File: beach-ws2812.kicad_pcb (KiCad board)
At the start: 4 copper layers, 260 x 120 mm, 343 parts, among them CON101 BARREL_JACK, P101 CONN_01X03, SW101 Pushbutton, SW102 Pushbutton, U101 STM32F103C(8-B)Tx, U102 LM1117-3.3, U103 MAX811, X101 8MHz

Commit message: Added mounting holes.
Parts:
- added C601: 100nF, Capacitors_SMD:C_0603, F.Cu at (238.4, 99.0)
- added C602: 100nF, Capacitors_SMD:C_0603, F.Cu at (255.6, 101.0)
- added C603: 100nF, Capacitors_SMD:C_0603, F.Cu at (261.2, 110.2)
- added C604: 100nF, Capacitors_SMD:C_0603, F.Cu at (268.8, 120.2)
- added C605: 100nF, Capacitors_SMD:C_0603, F.Cu at (277.8, 103.6)
- added C606: 100nF, Capacitors_SMD:C_0603, F.Cu at (277.4, 92.2)
- added C607: 100nF, Capacitors_SMD:C_0603, F.Cu at (262.0, 87.4)
- added C608: 100nF, Capacitors_SMD:C_0603, F.Cu at (244.6, 90.0)
- added C609: 100nF, Capacitors_SMD:C_0603, F.Cu at (249.6, 77.4)
- added C610: 100nF, Capacitors_SMD:C_0603, F.Cu at (270.4, 74.0)
- added C611: 100nF, Capacitors_SMD:C_0603, F.Cu at (263.6, 76.4)
- added C612: 100nF, Capacitors_SMD:C_0603, F.Cu at (271.6, 60.4)
- added C613: 100nF, Capacitors_SMD:C_0603, F.Cu at (264.0, 64.0)
- added HOLE1: MountingHole_3.2mm_M3, Mounting_Holes:MountingHole_3.2mm_M3, F.Cu at (27.0, 131.8)
- added HOLE2: MountingHole_3.2mm_M3, Mounting_Holes:MountingHole_3.2mm_M3, F.Cu at (27.0, 25.8)
- added HOLE3: MountingHole_3.2mm_M3, Mounting_Holes:MountingHole_3.2mm_M3, F.Cu at (273.0, 25.8)
- added HOLE4: MountingHole_3.2mm_M3, Mounting_Holes:MountingHole_3.2mm_M3, F.Cu at (273.0, 131.8)
- added LED601: WS2812B, LEDs:LED_WS2812B-PLCC4, F.Cu at (240.2, 103.6)
- added LED602: WS2812B, LEDs:LED_WS2812B-PLCC4, F.Cu at (250.0, 101.0)
- added LED603: WS2812B, LEDs:LED_WS2812B-PLCC4, F.Cu at (262.0, 104.6)
- added LED604: WS2812B, LEDs:LED_WS2812B-PLCC4, F.Cu at (267.0, 115.2)
- added LED605: WS2812B, LEDs:LED_WS2812B-PLCC4, F.Cu at (272.2, 102.8)
- added LED606: WS2812B, LEDs:LED_WS2812B-PLCC4, F.Cu at (272.0, 91.4)
- added LED607: WS2812B, LEDs:LED_WS2812B-PLCC4, F.Cu at (263.6, 92.4)
- added LED608: WS2812B, LEDs:LED_WS2812B-PLCC4, F.Cu at (250.2, 90.8)
- added LED609: WS2812B, LEDs:LED_WS2812B-PLCC4, F.Cu at (251.2, 82.2)
- added LED610: WS2812B, LEDs:LED_WS2812B-PLCC4, F.Cu at (272.0, 78.8)
- added LED611: WS2812B, LEDs:LED_WS2812B-PLCC4, F.Cu at (262.0, 71.2)
- added LED612: WS2812B, LEDs:LED_WS2812B-PLCC4, F.Cu at (271.6, 65.0)
- added LED613: WS2812B, LEDs:LED_WS2812B-PLCC4, F.Cu at (264.0, 59.2)
- moved C539 9.37 mm to (253.8, 122.0), turned to 90 degrees
- moved CON101 5.10 mm to (265.4, 131.2)
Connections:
- LED540 pad 2: Net-(LED540-Pad2) -> LEDDATA5
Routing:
- net +5V: track 1265.2 -> 1364.8 mm, vias 161 -> 174
- net GND: track 1334.7 -> 1409.2 mm, vias 171 -> 184
- net Net-(LED610-Pad2): track 0.00 -> 29.1 mm
- net Net-(LED608-Pad2): track 0.00 -> 19.0 mm
- net Net-(LED605-Pad2): track 0.00 -> 17.8 mm
- net LEDDATA5: track 0.00 -> 17.6 mm
- net Net-(LED609-Pad2): track 0.00 -> 15.9 mm
- net Net-(LED612-Pad2): track 0.00 -> 13.2 mm
- net Net-(LED603-Pad2): track 0.00 -> 11.4 mm
- net Net-(LED602-Pad2): track 0.00 -> 10.4 mm
- net Net-(LED607-Pad2): track 0.00 -> 10.4 mm
- net Net-(LED604-Pad2): track 0.00 -> 9.28 mm
- net Net-(LED611-Pad2): track 0.00 -> 5.84 mm
- net Net-(LED601-Pad2): track 0.00 -> 5.05 mm
- net Net-(LED606-Pad2): track 0.00 -> 4.31 mm
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
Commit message: Minor fixes after looking at printout. Added date as version marker.
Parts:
- G***: value LOGO -> LED placement
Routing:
- net +5V: track 1364.8 -> 1359.8 mm
- net GND: track 1409.2 -> 1412.6 mm
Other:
- board text added: "2018-05-09"

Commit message: Added big copper plane, warning about possible production problem from eurocircuits.
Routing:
- added copper zone on B.Cu, net (none)
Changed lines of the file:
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@@
   (layers
     (0 F.Cu signal)
-    (1 +5V power hide)
-    (2 GND power hide)
+    (1 +5V power)
+    (2 GND power)
     (31 B.Cu signal)
     (32 B.Adhes user)
@@
       )
     )
+  )
+  (zone (net 0) (net_name "") (layer B.Cu) (hatch edge 0.508)
+    (connect_pads (clearance 0.508))
+    (min_thickness 0.254)
+    (fill yes (arc_segments 16) (thermal_gap 0.508) (thermal_bridge_width 0.508))
+    (polygon
+      (pts
+        (xy 278 20.8) (xy 278 136.8) (xy 22 136.8) (xy 22 20.8)
+      )
+    )

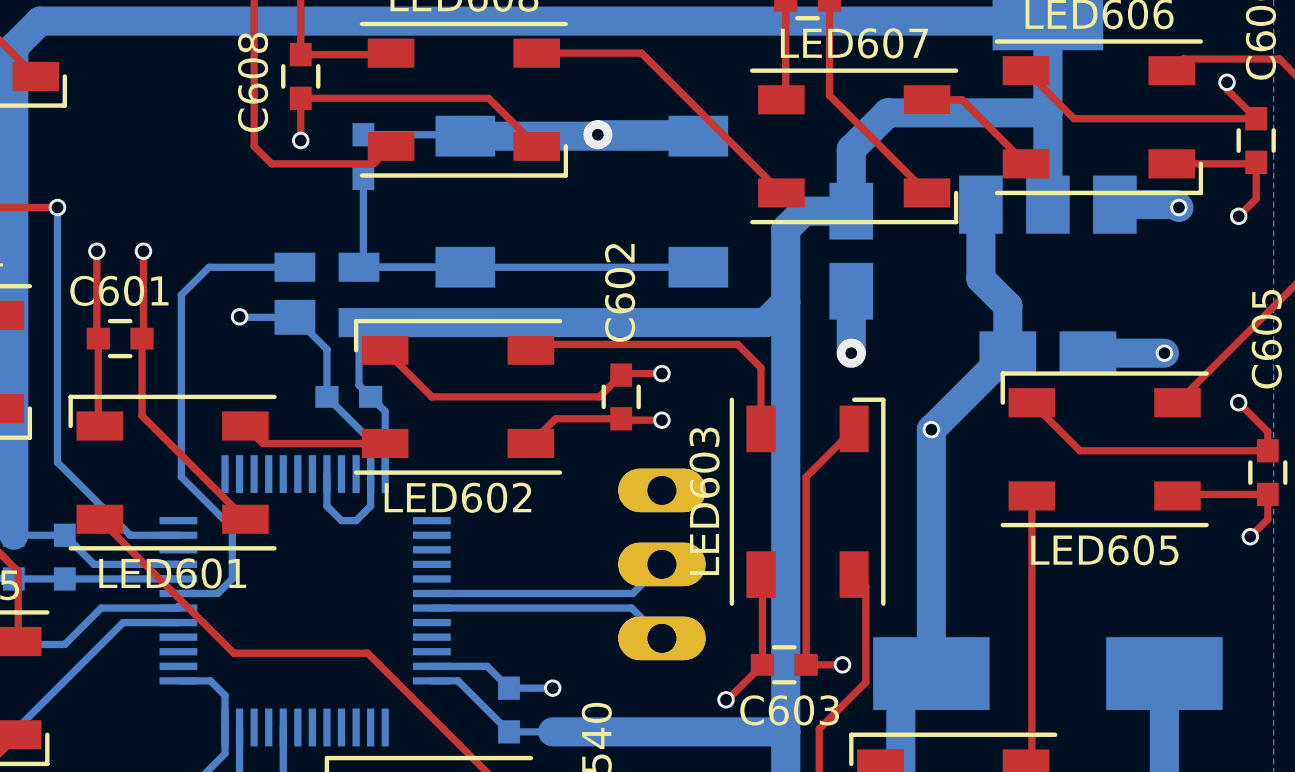
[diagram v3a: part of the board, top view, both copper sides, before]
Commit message: Changed tantalums on 3.3V regulator to size B.
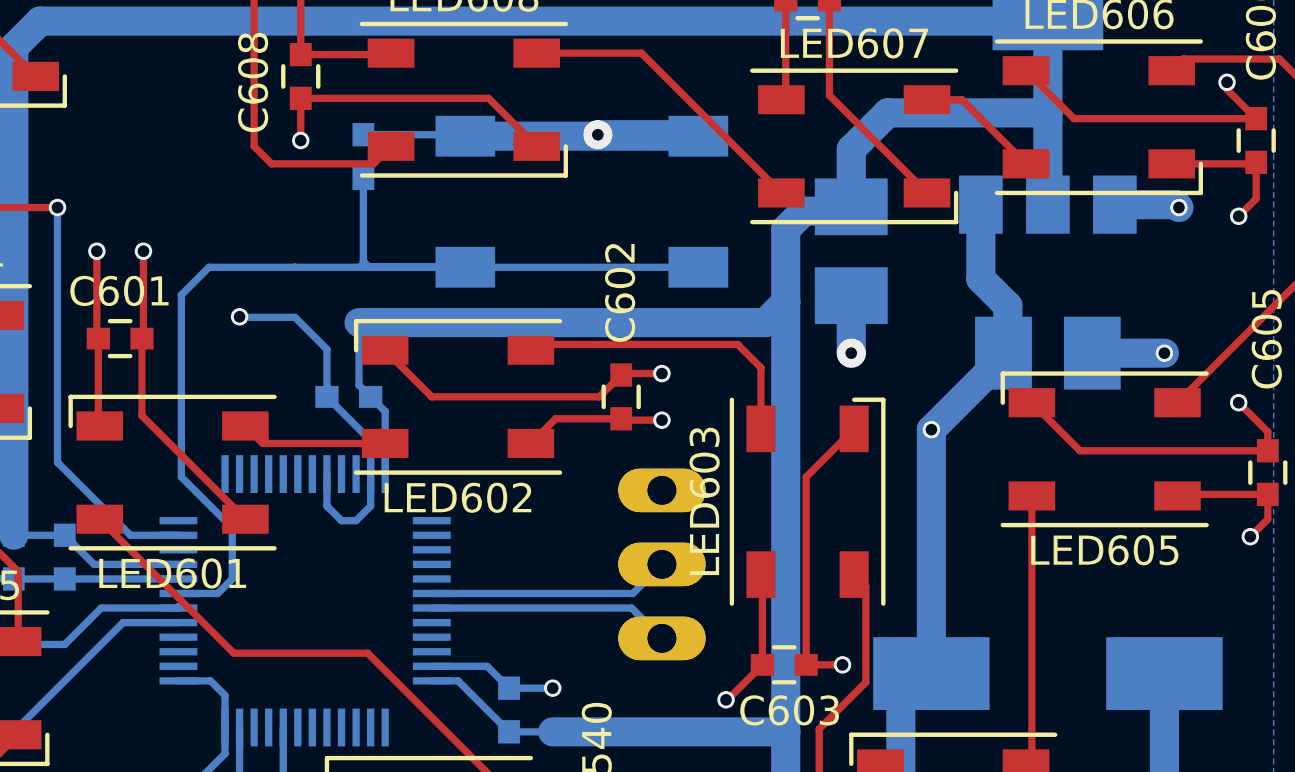
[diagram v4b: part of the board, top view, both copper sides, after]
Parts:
- removed U103: MAX811, TO_SOT_Packages_SMD:SOT-143
- C109, C110: footprint Capacitors_Tantalum_SMD:Tantalum_Case-A_EIA-3216-18_Reflow -> Capacitors_Tantalum_SMD:Tantalum_Case-B_EIA-3528-21_Reflow
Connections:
- U101 pad 7: Net-(U101-Pad7) -> Net-(C112-Pad2)
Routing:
- net Net-(C112-Pad2): track 18.1 -> 40.8 mm
- net Net-(U101-Pad7): track 16.8 -> 0.00 mm

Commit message: Added weak pull-ups to programming RX/TX pins.
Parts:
- added R103: 100K, Resistors_SMD:R_0603, B.Cu at (251.8, 105.8)
- added R104: 100K, Resistors_SMD:R_0603, B.Cu at (251.8, 109.1)
- moved C106 0.15 mm to (251.8, 111.9)
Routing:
- net +3V3: track 173.3 -> 188.5 mm
- net Net-(P101-Pad3): track 8.33 -> 15.2 mm
- net Net-(P101-Pad2): track 8.31 -> 9.51 mm
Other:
- board text added: "2018-05-21"
- board text removed: "2018-05-09"
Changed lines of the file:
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@@
 (kicad_pcb (version 4) (host pcbnew 4.0.5+dfsg1-4)
   (general
-    (links 921)
+    (links 925)
     (no_connects 0)
     (area 19.924999 18.674999 280.075001 138.825001)
     (thickness 1.6)
     (drawings 11)
-    (tracks 2509)
+    (tracks 2522)
     (zones 0)
-    (modules 372)
+    (modules 374)
     (nets 216)
   )
@@
   )
   (module Capacitors_SMD:C_0603 (layer B.Cu)
-    (at 251.75 111.75 90)
+    (at 251.75 111.9 90)
     (descr "Capacitor SMD 0603, reflow soldering, AVX (see smccp.pdf)")
     (tags "capacitor 0603")
     (attr smd)
-    (fp_text reference C106 (at 3.5 0 90) (layer B.SilkS)
+    (fp_text reference C106 (at -1.35 1.7 90) (layer B.SilkS)
       (effects (font (size 1 1) (thickness 0.15)) (justify mirror))
     )
@@
     )
   )
-  (gr_text 2018-05-09 (at 38.6 111.2) (layer F.SilkS)
+  (module Resistors_SMD:R_0603 (layer B.Cu)
+    (at 251.75 105.8 270)
+    (descr "Resistor SMD 0603, reflow soldering, Vishay (see dcrcw.pdf)")
+    (tags "resistor 0603")
+    (attr smd)
+    (fp_text reference R103 (at -0.6 -1.5 270) (layer B.SilkS)
+      (effects (font (size 1 1) (thickness 0.15)) (justify mirror))
+    )
+    (fp_text value 100K (at 0 -1.9 270) (layer B.Fab)
+      (effects (font (size 1 1) (thickness 0.15)) (justify mirror))
+    )
+    (fp_line (start -0.8 -0.4) (end -0.8 0.4) (layer B.Fab) (width 0.1))
+    (fp_line (start 0.8 -0.4) (end -0.8 -0.4) (layer B.Fab) (width 0.1))
+    (fp_line (start 0.8 0.4) (end 0.8 -0.4) (layer B.Fab) (width 0.1))
+    (fp_line (start -0.8 0.4) (end 0.8 0.4) (layer B.Fab) (width 0.1))
+    (fp_line (start -1.3 0.8) (end 1.3 0.8) (layer B.CrtYd) (width 0.05))
+    (fp_line (start -1.3 -0.8) (end 1.3 -0.8) (layer B.CrtYd) (width 0.05))
+    (fp_line (start -1.3 0.8) (end -1.3 -0.8) (layer B.CrtYd) (width 0.05))
+    (fp_line (start 1.3 0.8) (end 1.3 -0.8) (layer B.CrtYd) (width 0.05))
+    (fp_line (start 0.5 -0.675) (end -0.5 -0.675) (layer B.SilkS) (width 0.15))
+    (fp_line (start -0.5 0.675) (end 0.5 0.675) (layer B.SilkS) (width 0.15))
+    (pad 1 smd rect (at -0.75 0 270) (size 0.5 0.9) (layers B.Cu B.Paste B.Mask)
+      (net 4 +3V3))
+    (pad 2 smd rect (at 0.75 0 270) (size 0.5 0.9) (layers B.Cu B.Paste B.Mask)
+      (net 8 "Net-(P101-Pad2)"))
+    (model Resistors_SMD.3dshapes/R_0603.wrl
+      (at (xyz 0 0 0))
+      (scale (xyz 1 1 1))
+      (rotate (xyz 0 0 0))
+    )
+  )
+  (module Resistors_SMD:R_0603 (layer B.Cu)
+    (at 251.75 109.1 90)
+    (descr "Resistor SMD 0603, reflow soldering, Vishay (see dcrcw.pdf)")
+    (tags "resistor 0603")
+    (attr smd)
+    (fp_text reference R104 (at 0.25 1.45 90) (layer B.SilkS)
+      (effects (font (size 1 1) (thickness 0.15)) (justify mirror))
+    )
+    (fp_text value 100K (at 0 -1.9 90) (layer B.Fab)
+      (effects (font (size 1 1) (thickness 0.15)) (justify mirror))
+    )
+    (fp_line (start -0.8 -0.4) (end -0.8 0.4) (layer B.Fab) (width 0.1))
+    (fp_line (start 0.8 -0.4) (end -0.8 -0.4) (layer B.Fab) (width 0.1))
+    (fp_line (start 0.8 0.4) (end 0.8 -0.4) (layer B.Fab) (width 0.1))
+    (fp_line (start -0.8 0.4) (end 0.8 0.4) (layer B.Fab) (width 0.1))
+    (fp_line (start -1.3 0.8) (end 1.3 0.8) (layer B.CrtYd) (width 0.05))
+    (fp_line (start -1.3 -0.8) (end 1.3 -0.8) (layer B.CrtYd) (width 0.05))
+    (fp_line (start -1.3 0.8) (end -1.3 -0.8) (layer B.CrtYd) (width 0.05))
+    (fp_line (start 1.3 0.8) (end 1.3 -0.8) (layer B.CrtYd) (width 0.05))
+    (fp_line (start 0.5 -0.675) (end -0.5 -0.675) (layer B.SilkS) (width 0.15))
+    (fp_line (start -0.5 0.675) (end 0.5 0.675) (layer B.SilkS) (width 0.15))
+    (pad 1 smd rect (at -0.75 0 90) (size 0.5 0.9) (layers B.Cu B.Paste B.Mask)
+      (net 4 +3V3))
+    (pad 2 smd rect (at 0.75 0 90) (size 0.5 0.9) (layers B.Cu B.Paste B.Mask)
+      (net 9 "Net-(P101-Pad3)"))
+    (model Resistors_SMD.3dshapes/R_0603.wrl
+      (at (xyz 0 0 0))
+      (scale (xyz 1 1 1))
+      (rotate (xyz 0 0 0))
+    )
+  )
+  (gr_text 2018-05-21 (at 38.6 111.2) (layer F.SilkS)
     (effects (font (size 3 3) (thickness 0.3)))
   )
@@
   (segment (start 224.75 111.5) (end 228.4 111.5) (width 0.25) (layer B.Cu) (net 1) (status 30))
   (segment (start 228.4 111.5) (end 228.5 111.4) (width 0.25) (layer B.Cu) (net 1) (status 30))
+  (segment (start 251.75 111.15) (end 251.4 111.15) (width 0.25) (layer B.Cu) (net 2))
+  (segment (start 251.4 111.15) (end 250.5 110.25) (width 0.25) (layer B.Cu) (net 2))
+  (segment (start 250.5 110.25) (end 249.1 110.25) (width 0.25) (layer B.Cu) (net 2))
   (segment (start 277.4 92.95) (end 277.4 94.2) (width 0.25) (layer F.Cu) (net 2))
   (via (at 276.8 94.8) (size 0.6) (drill 0.4) (layers F.Cu B.Cu) (net 2))
@@
   (segment (start 245.5 99.36944) (end 245.5 101) (width 0.25) (layer B.Cu) (net 2) (status 20))
   (segment (start 241.75 115) (end 241.75 116.75) (width 0.25) (layer B.Cu) (net 2) (status 30))
-  (segment (start 251.75 111) (end 251 110.25) (width 0.25) (layer B.Cu) (net 2) (status 10))
-  (segment (start 251 110.25) (end 249.1 110.25) (width 0.25) (layer B.Cu) (net 2) (status 20))
   (segment (start 236.5 107.25) (end 234.75 107.25) (width 0.25) (layer B.Cu) (net 2) (status 30))
   (segment (start 236.5 107.25) (end 240.4 107.25) (width 0.25) (layer B.Cu) (net 2) (status 30))
@@
   (segment (start 231 105.1) (end 231 101.75) (width 0.25) (layer B.Cu) (net 3) (status 10))
   (segment (start 231 101.75) (end 230.5 101.25) (width 0.25) (layer B.Cu) (net 3) (status 20))
+  (segment (start 251.75 105.05) (end 253.95 105.05) (width 0.25) (layer B.Cu) (net 4))
+  (segment (start 254.35 105.45) (end 261.25 105.45) (width 0.25) (layer B.Cu) (net 4))
+  (segment (start 253.95 105.05) (end 254.35 105.45) (width 0.25) (layer B.Cu) (net 4))
+  (segment (start 251.75 109.85) (end 254.45 109.85) (width 0.25) (layer B.Cu) (net 4))
+  (segment (start 254.9 110.3) (end 254.9 112.5) (width 0.25) (layer B.Cu) (net 4))
+  (segment (start 254.45 109.85) (end 254.9 110.3) (width 0.25) (layer B.Cu) (net 4))
   (segment (start 270.25 88.1) (end 235.65 88.1) (width 1) (layer B.Cu) (net 4))
   (segment (start 234.75 89) (end 234.75 105.75) (width 1) (layer B.Cu) (net 4))
   (segment (start 235.65 88.1) (end 234.75 89) (width 1) (layer B.Cu) (net 4))
-  (segment (start 261.25 112.5) (end 253.25 112.5) (width 1) (layer B.Cu) (net 4))
+  (segment (start 261.25 112.5) (end 254.9 112.5) (width 1) (layer B.Cu) (net 4))
+  (segment (start 254.9 112.5) (end 253.25 112.5) (width 1) (layer B.Cu) (net 4))
   (segment (start 253.25 112.5) (end 251.75 112.5) (width 0.25) (layer B.Cu) (net 4) (status 20))
   (segment (start 240.25 116.75) (end 240.25 118.25) (width 0.25) (layer B.Cu) (net 4) (status 10))
@@
   (segment (start 260.2 122.3) (end 261.25 121.25) (width 1) (layer B.Cu) (net 4))
   (segment (start 261.25 121.25) (end 261.25 112.5) (width 1) (layer B.Cu) (net 4))
-  (segment (start 261.25 112.5) (end 261.25 97.75) (width 1) (layer B.Cu) (net 4))
+  (segment (start 261.25 112.5) (end 261.25 105.45) (width 1) (layer B.Cu) (net 4))
+  (segment (start 261.25 105.45) (end 261.25 97.75) (width 1) (layer B.Cu) (net 4))
   (segment (start 247 101) (end 247.5 101.5) (width 0.25) (layer B.Cu) (net 4) (status 10))
   (segment (start 247.5 101.5) (end 247.5 103.65) (width 0.25) (layer B.Cu) (net 4) (status 20))
@@
   (segment (start 233 94.5) (end 173 34.5) (width 0.25) (layer B.Cu) (net 7))
   (segment (start 173 34.5) (end 32.5 34.5) (width 0.25) (layer B.Cu) (net 7))
+  (segment (start 251.75 107.75) (end 251.75 106.55) (width 0.25) (layer B.Cu) (net 8))
   (segment (start 257 106.75) (end 256 107.75) (width 0.25) (layer B.Cu) (net 8) (status 10))
-  (segment (start 256 107.75) (end 249.1 107.75) (width 0.25) (layer B.Cu) (net 8) (status 20))
-  (segment (start 257 109.29) (end 255.96 108.25) (width 0.25) (layer B.Cu) (net 9) (status 10))
+  (segment (start 256 107.75) (end 251.75 107.75) (width 0.25) (layer B.Cu) (net 8) (status 20))
+  (segment (start 251.75 107.75) (end 249.1 107.75) (width 0.25) (layer B.Cu) (net 8) (status 20))
+  (segment (start 251.75 108.25) (end 249.1 108.25) (width 0.25) (layer B.Cu) (net 9))
+  (segment (start 257 109.29) (end 255.96 108.25) (width 0.25) (layer B.Cu) (net 9))
+  (segment (start 255.96 108.25) (end 251.75 108.25) (width 0.25) (layer B.Cu) (net 9))
   (segment (start 255.96 108.25) (end 249.1 108.25) (width 0.25) (layer B.Cu) (net 9) (status 20))
   (segment (start 244 112.35) (end 244 116.25) (width 0.25) (layer B.Cu) (net 10))

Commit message: Rotated power connector, now to the side. Updated time stamp.
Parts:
- moved CON101 10.5 mm to (272.5, 123.4), turned to 180 degrees
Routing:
- net +5V: track 1359.8 -> 1364.7 mm, vias 174 -> 177
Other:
- board text added: "2018-05-27"
- board text removed: "2018-05-21"
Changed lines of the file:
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@@
     (links 925)
     (no_connects 0)
-    (area 19.924999 18.674999 280.075001 138.825001)
+    (area 9.435716 14.8 282.557143 139.275)
     (thickness 1.6)
     (drawings 11)
-    (tracks 2522)
+    (tracks 2527)
     (zones 0)
     (modules 374)
@@
   )
   (setup
-    (last_trace_width 0.25)
+    (last_trace_width 1)
     (user_trace_width 1)
     (trace_clearance 0.2)
@@
   )
   (module Connect:BARREL_JACK (layer B.Cu)
-    (at 265.4 131.2 90)
+    (at 272.5 123.4 180)
     (descr "DC Barrel Jack")
     (tags "Power Jack")
-    (fp_text reference CON101 (at 6.4 7.8 360) (layer B.SilkS)
+    (fp_text reference CON101 (at 6.4 7.8 450) (layer B.SilkS)
       (effects (font (size 1 1) (thickness 0.15)) (justify mirror))
     )
-    (fp_text value BARREL_JACK (at 0 5.99948 90) (layer B.Fab)
+    (fp_text value BARREL_JACK (at 0 5.99948 180) (layer B.Fab)
       (effects (font (size 1 1) (thickness 0.15)) (justify mirror))
     )
@@
     (fp_line (start 7.00024 -4.50088) (end 7.00024 4.50088) (layer B.SilkS) (width 0.15))
     (fp_line (start 7.00024 4.50088) (end -7.50062 4.50088) (layer B.SilkS) (width 0.15))
-    (pad 1 thru_hole rect (at 6.20014 0 90) (size 3.50012 3.50012) (drill oval 1.00076 2.99974) (layers *.Cu *.Mask)
-      (net 5 +5V))
-    (pad 2 thru_hole rect (at 0.20066 0 90) (size 3.50012 3.50012) (drill oval 1.00076 2.99974) (layers *.Cu *.Mask)
+    (pad 1 thru_hole rect (at 6.20014 0 180) (size 3.50012 3.50012) (drill oval 1.00076 2.99974) (layers *.Cu *.Mask)
+      (net 5 +5V) (zone_connect 0))
+    (pad 2 thru_hole rect (at 0.20066 0 180) (size 3.50012 3.50012) (drill oval 1.00076 2.99974) (layers *.Cu *.Mask)
       (net 2 GND))
-    (pad 3 thru_hole rect (at 3.2004 -4.699 90) (size 3.50012 3.50012) (drill oval 2.99974 1.00076) (layers *.Cu *.Mask)
+    (pad 3 thru_hole rect (at 3.2004 -4.699 180) (size 3.50012 3.50012) (drill oval 2.99974 1.00076) (layers *.Cu *.Mask)
       (net 2 GND))
   )
@@
     )
   )
-  (gr_text 2018-05-21 (at 38.6 111.2) (layer F.SilkS)
+  (gr_text 2018-05-27 (at 38.6 111.2) (layer F.SilkS)
     (effects (font (size 3 3) (thickness 0.3)))
   )
@@
   (segment (start 44 108.2) (end 24 108.2) (width 0.25) (layer +5V) (net 0))
   (segment (start 44 102.8) (end 44 108.2) (width 0.25) (layer +5V) (net 0))
+  (segment (start 260.2 129.4) (end 260 129.4) (width 0.25) (layer GND) (net 0))
+  (segment (start 261.8 129.4) (end 262 129.4) (width 0.25) (layer +5V) (net 0))
   (segment (start 229.5 113.25) (end 234 113.25) (width 0.25) (layer B.Cu) (net 1))
   (segment (start 234 113.25) (end 238.5 108.75) (width 0.25) (layer B.Cu) (net 1))
@@
   (via (at 53.4 22) (size 0.6) (drill 0.4) (layers F.Cu B.Cu) (net 2))
   (segment (start 54.4 21) (end 53.4 22) (width 0.25) (layer F.Cu) (net 2))
-  (segment (start 260.2 129.4) (end 260 129.4) (width 0.25) (layer GND) (net 2))
-  (segment (start 261.8 129.4) (end 262 129.4) (width 0.25) (layer +5V) (net 2))
   (segment (start 253.8 121.25) (end 252.45 121.25) (width 0.25) (layer F.Cu) (net 2))
   (segment (start 252.4 121.2) (end 252.2 121.2) (width 0.25) (layer GND) (net 2))
@@
   (segment (start 270.25 88.1) (end 270.25 91.25) (width 1) (layer B.Cu) (net 4) (status 10))
   (segment (start 270.25 91.25) (end 270.25 94.4) (width 1) (layer B.Cu) (net 4) (status 20))
+  (segment (start 266.25 108.15) (end 266.25 106.15) (width 1) (layer B.Cu) (net 5))
+  (via (at 266.25 106.15) (size 0.6) (drill 0.4) (layers F.Cu B.Cu) (net 5))
+  (segment (start 266.25 104.15) (end 266.25 102.125) (width 1) (layer B.Cu) (net 5))
+  (via (at 266.25 104.15) (size 0.6) (drill 0.4) (layers F.Cu B.Cu) (net 5))
+  (segment (start 266.25 106.15) (end 266.25 104.15) (width 1) (layer B.Cu) (net 5))
+  (via (at 266.25 108.15) (size 0.6) (drill 0.4) (layers F.Cu B.Cu) (net 5))
+  (segment (start 266.25 110.5) (end 265 111.75) (width 1) (layer B.Cu) (net 5))
+  (segment (start 265 111.75) (end 265 122.10014) (width 1) (layer B.Cu) (net 5))
+  (segment (start 265 122.10014) (end 266.29986 123.4) (width 1) (layer B.Cu) (net 5))
   (segment (start 181.2 21.45) (end 179.95 21.45) (width 0.25) (layer F.Cu) (net 5))
   (via (at 178.4 23) (size 0.6) (drill 0.4) (layers F.Cu B.Cu) (net 5))
@@
   (via (at 125.6 22.4) (size 0.6) (drill 0.4) (layers F.Cu B.Cu) (net 5))
   (segment (start 127 21) (end 125.6 22.4) (width 0.25) (layer F.Cu) (net 5))
-  (segment (start 265.4 124.99986) (end 265.2 124.79986) (width 1) (layer B.Cu) (net 5))
-  (segment (start 265.2 124.79986) (end 265.2 111.55) (width 1) (layer B.Cu) (net 5))
-  (segment (start 265.2 111.55) (end 266.25 110.5) (width 1) (layer B.Cu) (net 5))
-  (segment (start 265.801 125.301) (end 265.75 125.25) (width 1) (layer GND) (net 5))
   (segment (start 253.8 122.75) (end 253.8 124.2) (width 0.25) (layer F.Cu) (net 5))
   (segment (start 253.8 124.2) (end 253.6 124.2) (width 0.25) (layer +5V) (net 5))
